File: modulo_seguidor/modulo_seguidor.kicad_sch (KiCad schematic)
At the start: 30 parts, among them J1 Battery, J2 Motor A Entradas, J3 Motor B Entradas, J4 Motor A Salidas, J5 Motor B Salidas, J6 puerto sensores, M1 Motor_IZQ, M2 Motor_DER, SW1 SW_Push, SW2 SW_Nidec_CAS-120A1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

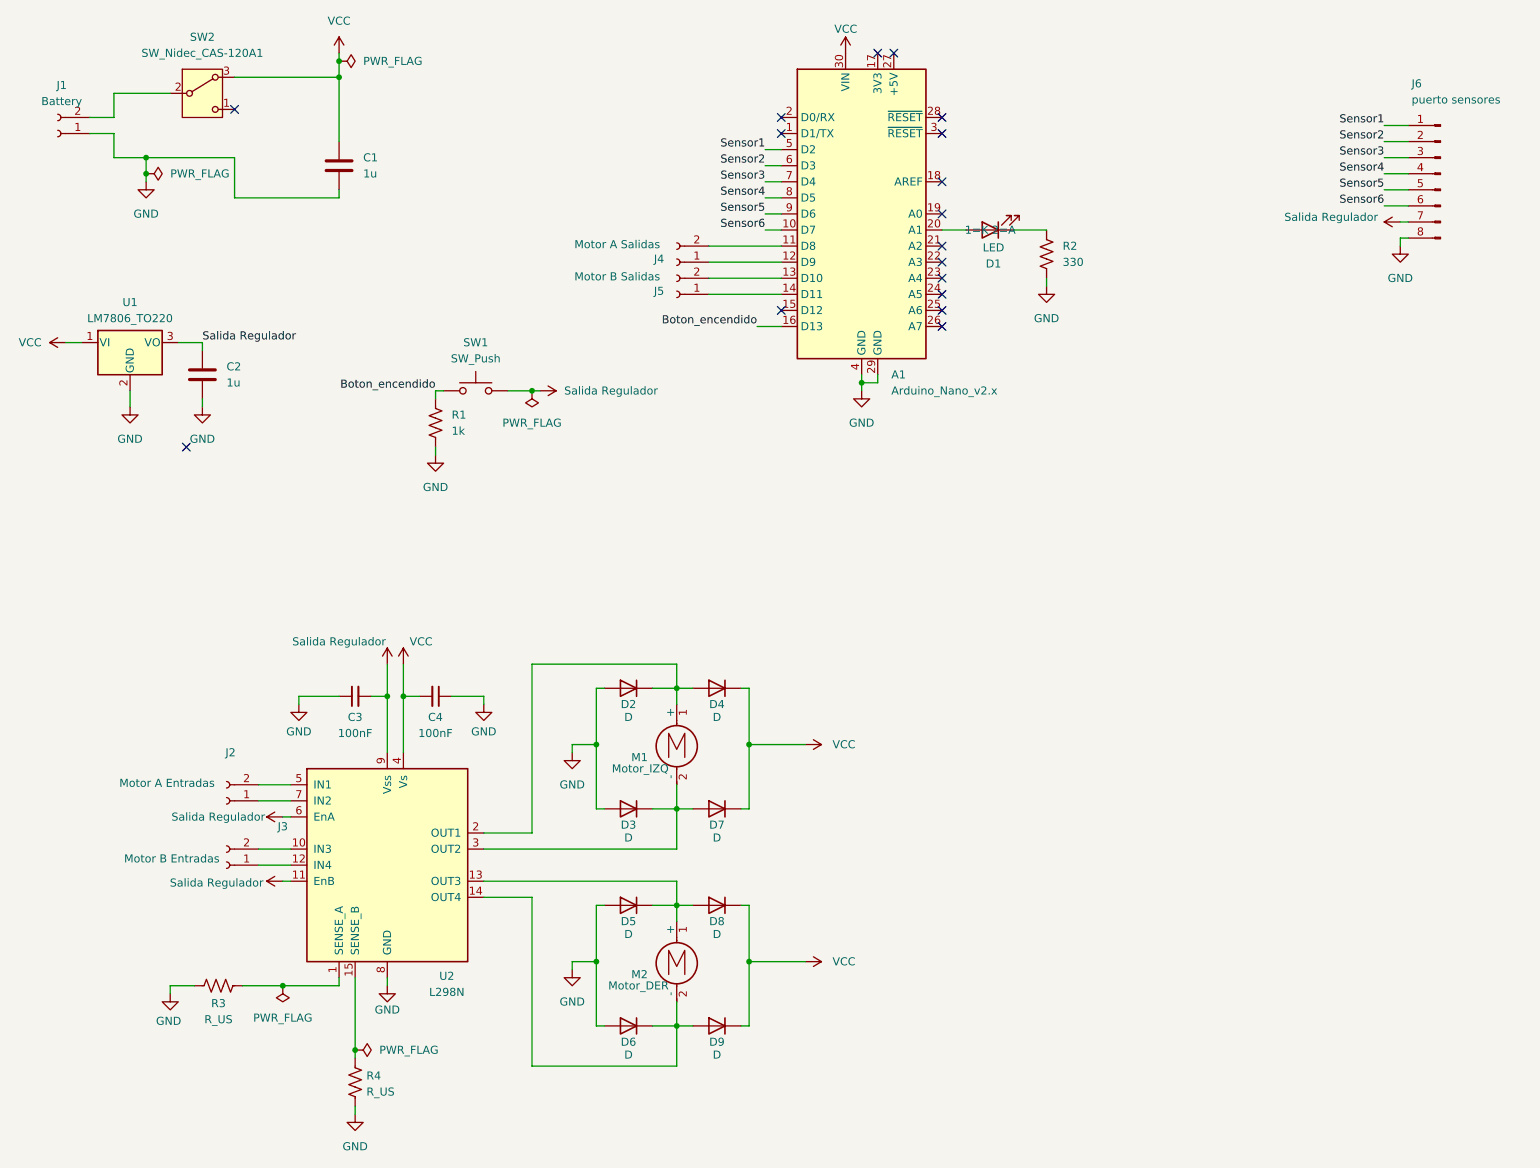
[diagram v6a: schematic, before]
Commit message: refactor!(Modulo seguidor): Cambio pines de sensores a analógicos, PWM, pin de botón, y led
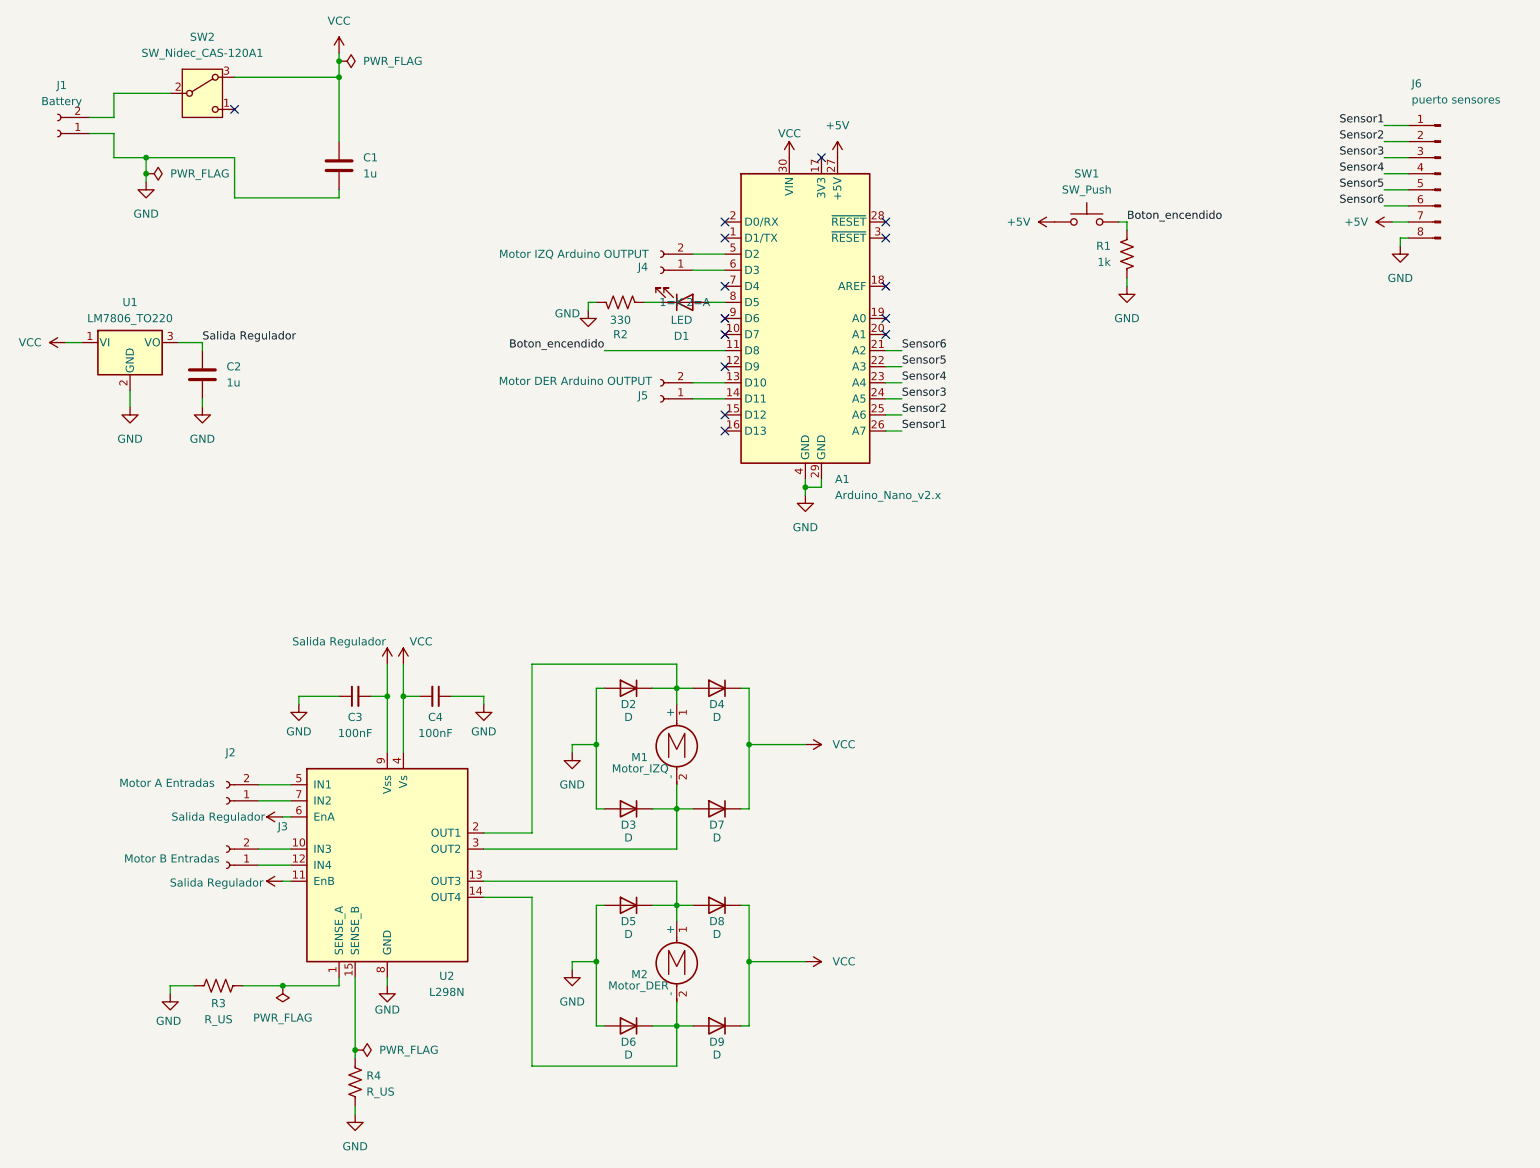
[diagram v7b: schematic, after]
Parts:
- J4: value Motor A Salidas -> Motor IZQ Arduino OUTPUT
- J5: value Motor B Salidas -> Motor DER Arduino OUTPUT
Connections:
- net Boton_encendido: now also A1.11 (D8); no longer A1.16 (D13)
- net GND: now also R2.1; no longer R2.2
- net Salida Regulador: no longer J6.7 (Pin_7), SW1.1
- net Sensor1: now also A1.26 (A7); no longer A1.5 (D2)
- net Sensor2: now also A1.25 (A6); no longer A1.6 (D3)
- net Sensor3: now also A1.24 (A5); no longer A1.7 (D4)
- net Sensor4: now also A1.23 (A4); no longer A1.8 (D5)
- net Sensor5: now also A1.22 (A3); no longer A1.9 (D6)
- net Sensor6: now also A1.21 (A2); no longer A1.10 (D7)
- net at J4.1 (Pin_1): now also A1.6 (D3); no longer A1.12 (D9)
- net at J4.2 (Pin_2): now also A1.5 (D2); no longer A1.11 (D8)
- net at D1.1 (K): now also R2.2; no longer R2.1
- net at D1.2 (A): now also A1.8 (D5); no longer A1.20 (A1)
- net +5V: now reaches A1.27 (+5V)
- net +5V: now also J6.7 (Pin_7), SW1.1
- no-connect marks 17 -> 15
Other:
- moved on the sheet: A1, D1, J4, J5, R1, R2, SW1

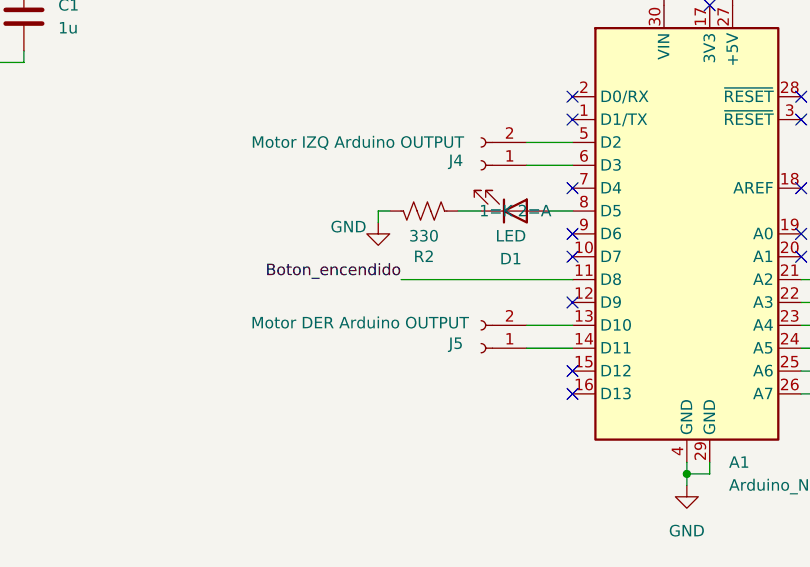
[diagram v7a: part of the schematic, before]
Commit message: refactor(modulo-seguidor): Cambio pines de led y de boton del seguidor
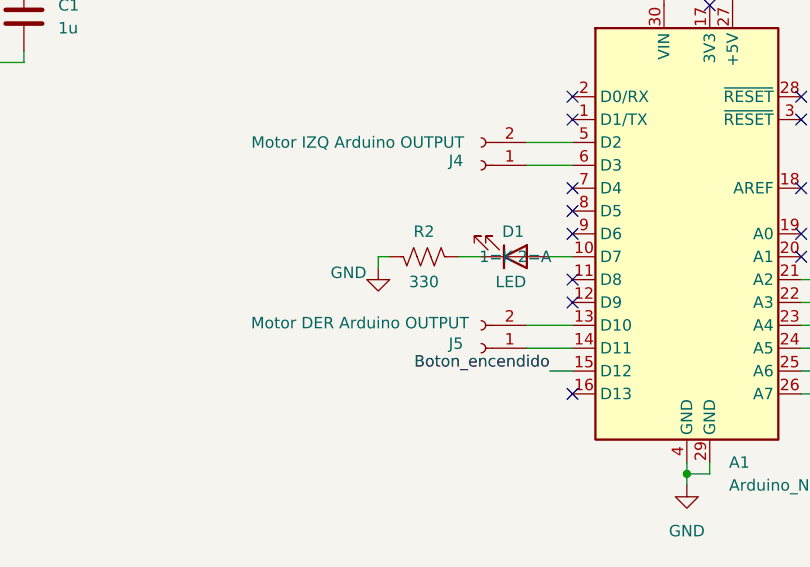
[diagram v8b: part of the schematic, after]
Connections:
- net Boton_encendido: now also A1.15 (D12); no longer A1.11 (D8)
- net at D1.2 (A): now also A1.10 (D7); no longer A1.8 (D5)
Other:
- moved on the sheet: D1, R2
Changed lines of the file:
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@@
 	)
 	(no_connect
-		(at 133.35 64.77)
+		(at 133.35 62.23)
+	)
+	(no_connect
+		(at 133.35 67.31)
 	)
 	(no_connect
@@
 	)
 	(no_connect
-		(at 148.59 36.83)
+		(at 133.35 59.69)
 	)
 	(no_connect
-		(at 158.75 46.99)
+		(at 148.59 36.83)
 	)
 	(no_connect
-		(at 133.35 77.47)
+		(at 158.75 46.99)
 	)
 	(no_connect
@@
 		(at 55.88 29.21)
 	)
-	(no_connect
-		(at 133.35 62.23)
-	)
 	(wire
 		(pts
@@
 	(wire
 		(pts
-			(xy 130.81 59.69) (xy 133.35 59.69)
+			(xy 130.81 64.77) (xy 133.35 64.77)
 		)
 		(stroke
@@
 	(wire
 		(pts
-			(xy 114.3 67.31) (xy 133.35 67.31)
+			(xy 130.81 77.47) (xy 133.35 77.47)
 		)
 		(stroke
@@
 	(wire
 		(pts
-			(xy 111.76 59.69) (xy 111.76 60.96)
+			(xy 111.76 64.77) (xy 111.76 66.04)
 		)
 		(stroke
@@
 	(wire
 		(pts
-			(xy 123.19 59.69) (xy 120.65 59.69)
+			(xy 123.19 64.77) (xy 120.65 64.77)
 		)
 		(stroke
@@
 	(wire
 		(pts
-			(xy 113.03 59.69) (xy 111.76 59.69)
+			(xy 113.03 64.77) (xy 111.76 64.77)
 		)
 		(stroke
@@
 	)
 	(label "Boton_encendido"
-		(at 114.3 67.31 180)
+		(at 130.81 77.47 180)
 		(effects
 			(font
@@
 	(symbol
 		(lib_id "Device:LED")
-		(at 127 59.69 0)
+		(at 127 64.77 0)
 		(mirror x)
 		(unit 1)
@@
 		(dnp no)
 		(property "Reference" "D1"
-			(at 126.492 65.024 0)
+			(at 126.746 61.976 0)
 			(effects
 				(font
@@
 		)
 		(property "Value" "LED"
-			(at 126.492 62.484 0)
+			(at 126.492 67.564 0)
 			(effects
 				(font
@@
 		)
 		(property "Footprint" "LED_THT:LED_D5.0mm"
-			(at 127 59.69 0)
+			(at 127 64.77 0)
 			(effects
 				(font
@@
 		)
 		(property "Datasheet" "~"
-			(at 127 59.69 0)
+			(at 127 64.77 0)
 			(effects
 				(font
@@
 		)
 		(property "Description" "Light emitting diode"
-			(at 127 59.69 0)
+			(at 127 64.77 0)
 			(effects
 				(font
@@
 		)
 		(property "Sim.Pins" "1=K 2=A"
-			(at 127 59.69 0)
+			(at 127 64.77 0)
 			(effects
 				(font
@@
 	(symbol
 		(lib_id "Device:R_US")
-		(at 116.84 59.69 90)
+		(at 116.84 64.77 90)
 		(mirror x)
 		(unit 1)
@@
 		(dnp no)
 		(property "Reference" "R2"
-			(at 116.84 64.77 90)
+			(at 116.84 61.976 90)
 			(effects
 				(font
@@
 		)
 		(property "Value" "330"
-			(at 116.84 62.484 90)
+			(at 116.84 67.564 90)
 			(effects
 				(font
@@
 		)
 		(property "Footprint" "Resistor_SMD:R_1206_3216Metric_Pad1.30x1.75mm_HandSolder"
-			(at 117.094 60.706 90)
+			(at 117.094 65.786 90)
 			(effects
 				(font
@@
 		)
 		(property "Datasheet" "~"
-			(at 116.84 59.69 0)
+			(at 116.84 64.77 0)
 			(effects
 				(font
@@
 		)
 		(property "Description" "Resistor, US symbol"
-			(at 116.84 59.69 0)
+			(at 116.84 64.77 0)
 			(effects
 				(font
@@
 	(symbol
 		(lib_id "power:GND")
-		(at 111.76 60.96 0)
+		(at 111.76 66.04 0)
 		(mirror y)
 		(unit 1)
@@
 		(dnp no)
 		(property "Reference" "#PWR06"
-			(at 111.76 67.31 0)
+			(at 111.76 72.39 0)
 			(effects
 				(font
@@
 		)
 		(property "Value" "GND"
-			(at 108.458 61.468 0)
+			(at 108.458 66.548 0)
 			(effects
 				(font
@@
 		)
 		(property "Footprint" ""
-			(at 111.76 60.96 0)
+			(at 111.76 66.04 0)
 			(effects
 				(font
@@
 		)
 		(property "Datasheet" ""
-			(at 111.76 60.96 0)
+			(at 111.76 66.04 0)
 			(effects
 				(font
@@
 		)
 		(property "Description" "Power symbol creates a global label with name \"GND\" , ground"
-			(at 111.76 60.96 0)
+			(at 111.76 66.04 0)
 			(effects
 				(font
